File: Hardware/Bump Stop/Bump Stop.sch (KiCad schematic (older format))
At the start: 14 parts, among them J1 Screw_Terminal_01x03, J2 Screw_Terminal_01x02, J3 PASS1, J4 PASS2, J5 FAIL1, J6 FAIL2, SW1 ADDRESS, U1 WeMos_mini

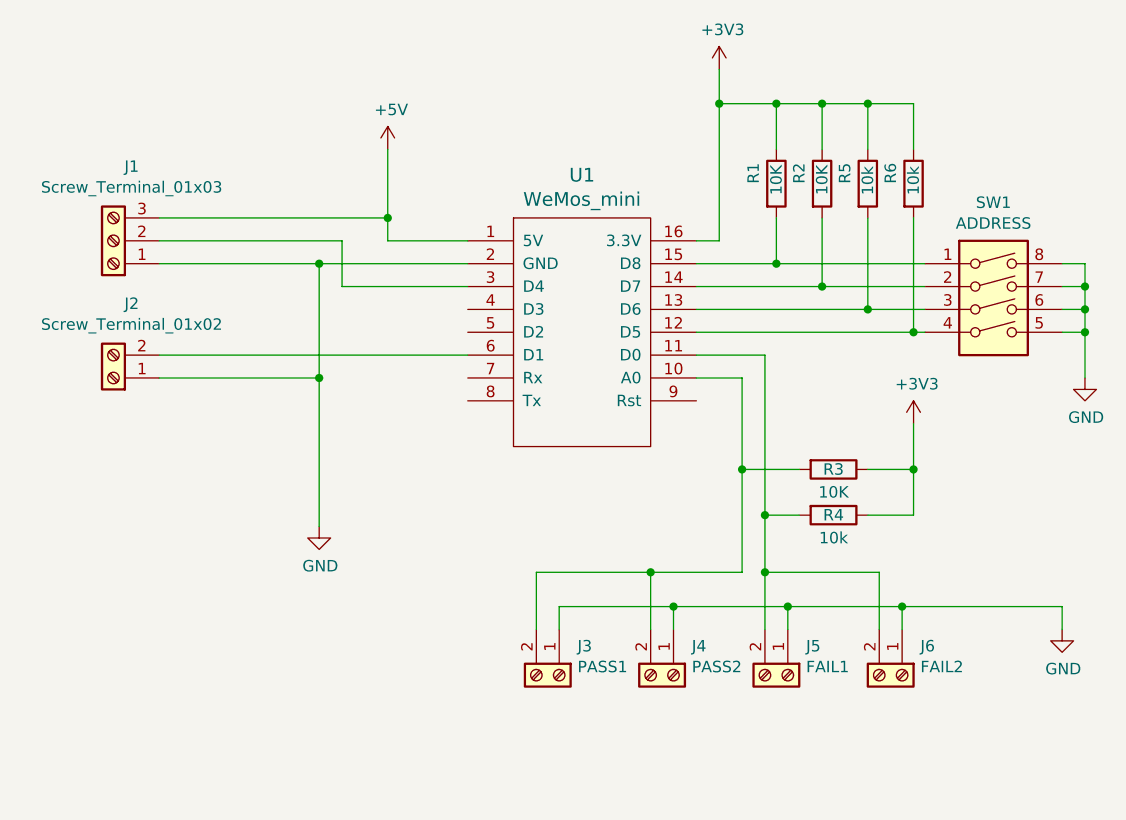
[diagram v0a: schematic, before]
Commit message: Updates to the bump sensor sketch and schematics
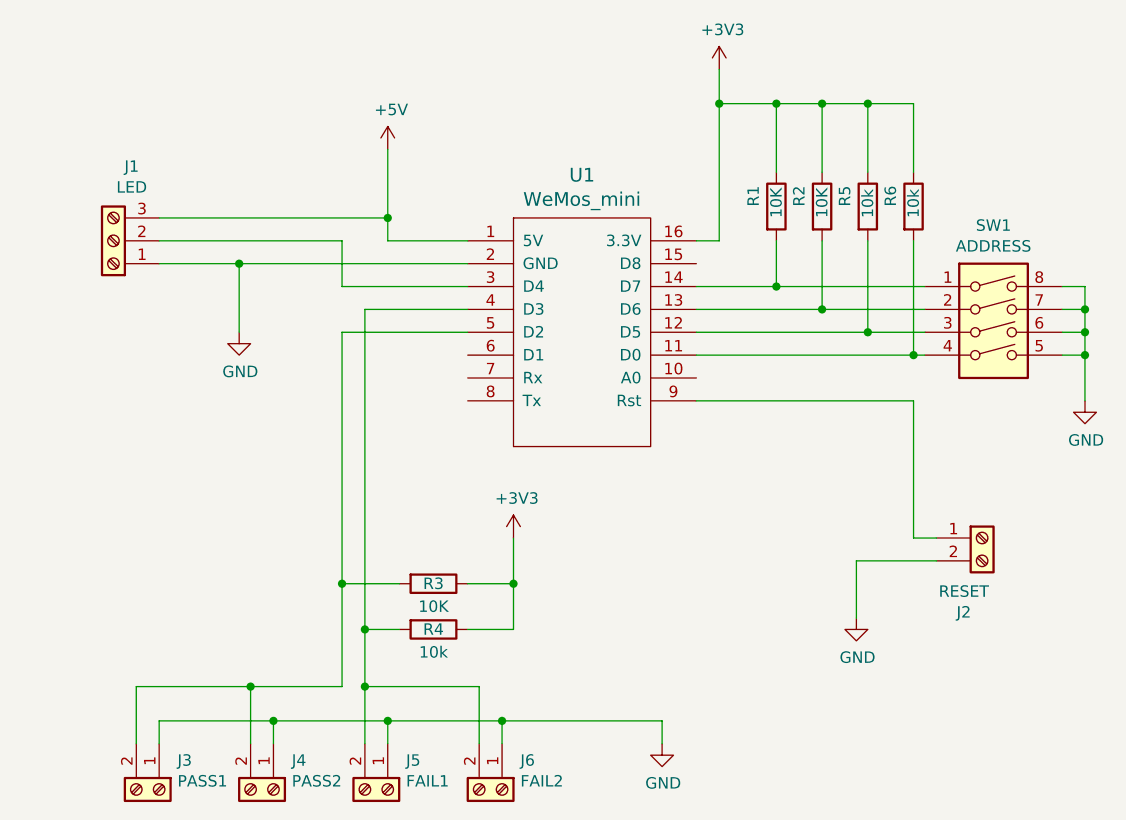
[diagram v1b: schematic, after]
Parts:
- J1: value Screw_Terminal_01x03 -> LED
- J2: value Screw_Terminal_01x02 -> RESET
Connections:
- net GND: now also J2.2 (Pin_2); no longer J2.1 (Pin_1)
- net at J3.2 (Pin_2), J4.2 (Pin_2), R3.2: now also U1.5 (D2); no longer U1.10 (A0)
- net at J5.2 (Pin_2), J6.2 (Pin_2), R4.2: now also U1.4 (D3); no longer U1.11 (D0)
- net at R6.2, SW1.4: now also U1.11 (D0); no longer U1.12 (D5)
- net at R5.2, SW1.3: now also U1.12 (D5); no longer U1.13 (D6)
- net at R2.2, SW1.2: now also U1.13 (D6); no longer U1.14 (D7)
- net at R1.2, SW1.1: now also U1.14 (D7); no longer U1.15 (D8)
- net at U1.6 (D1): no longer J2.2 (Pin_2)
- net at U1.9 (Rst): now also J2.1 (Pin_1)
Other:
- moved on the sheet: J2, J3, J4, J5, J6, R1, R2, R3, R4, R5, R6, SW1
